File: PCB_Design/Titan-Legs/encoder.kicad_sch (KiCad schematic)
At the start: 2 parts, among them U2 AS5047P-ATSM

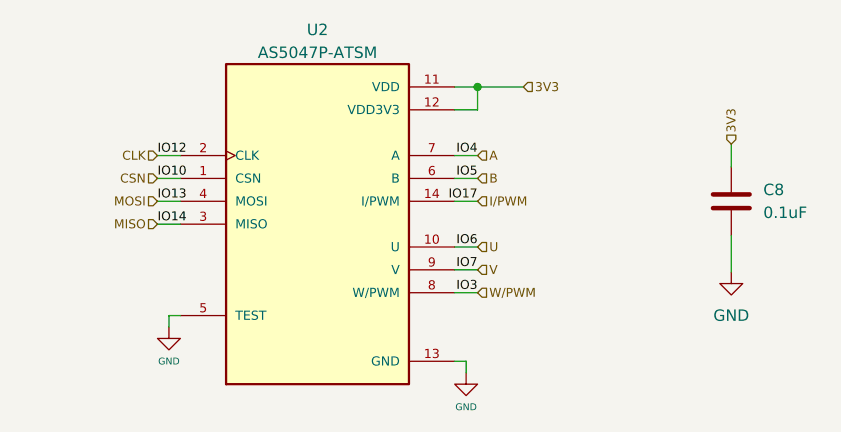
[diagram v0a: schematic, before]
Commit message: Copper filled VM to mosfets
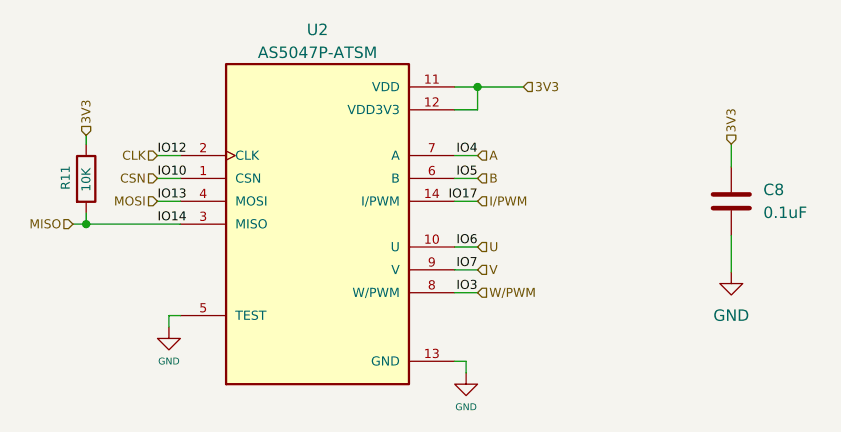
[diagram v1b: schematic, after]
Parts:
- added R11: 10K, Resistor_SMD:R_0603_1608Metric, symbol Device:R
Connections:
- net 3V3: now also R11.1
- net MISO: now also R11.2
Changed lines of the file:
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@@
   (junction (at 139.7 77.47) (diameter 0) (color 0 0 0 0)
   )
+  (junction (at 96.2152 92.71) (diameter 0) (color 0 0 0 0)
+  )
   (wire (pts (xy 105.41 102.87) (xy 105.41 104.14))
     (stroke (width 0) (type default) (color 0 0 0 0))
@@
     (stroke (width 0) (type default) (color 0 0 0 0))
   )
+  (wire (pts (xy 96.2152 82.8548) (xy 96.2152 83.8708))
+    (stroke (width 0) (type default) (color 0 0 0 0))
+  )
   (wire (pts (xy 139.7 77.47) (xy 144.78 77.47))
     (stroke (width 0) (type default) (color 0 0 0 0))
@@
     (stroke (width 0) (type default) (color 0 0 0 0))
   )
-  (wire (pts (xy 104.14 92.71) (xy 106.68 92.71))
+  (wire (pts (xy 96.2152 91.4908) (xy 96.2152 92.71))
+    (stroke (width 0) (type default) (color 0 0 0 0))
+  )
+  (wire (pts (xy 94.742 92.71) (xy 96.2152 92.71))
     (stroke (width 0) (type default) (color 0 0 0 0))
   )
@@
     (stroke (width 0) (type default) (color 0 0 0 0))
   )
+  (wire (pts (xy 96.2152 92.71) (xy 106.68 92.71))
+    (stroke (width 0) (type default) (color 0 0 0 0))
+  )
   (wire (pts (xy 138.43 107.95) (xy 138.43 109.22))
     (stroke (width 0) (type default) (color 0 0 0 0))
@@
     (effects (font (size 1 1)) (justify left))
   )
+  (hierarchical_label "3V3" (shape input) (at 96.2152 82.8548 90)
+    (effects (font (size 1 1)) (justify left))
+  )
   (hierarchical_label "3V3" (shape input) (at 144.78 77.47 0)
     (effects (font (size 1 1)) (justify left))
@@
     (effects (font (size 1 1)) (justify left))
   )
-  (hierarchical_label "MISO" (shape input) (at 104.14 92.71 180)
+  (hierarchical_label "MISO" (shape input) (at 94.742 92.71 180)
     (effects (font (size 1 1)) (justify right))
   )
@@
     (pin "1")
   )
+  (symbol (lib_id "Device:R") (at 96.2152 87.6808 0) (unit 1)
+    (in_bom yes) (on_board yes)
+    (property "Reference" "R11" (id 0) (at 93.9292 88.9 90)
+      (effects (font (size 1 1)) (justify left))
+    )
+    (property "Value" "10K" (id 1) (at 96.2152 89.1032 90)
+      (effects (font (size 1 1)) (justify left))
+    )
+    (property "Footprint" "Resistor_SMD:R_0603_1608Metric" (id 2) (at 94.4372 87.6808 90)
+      (effects (font (size 1.27 1.27)) hide)
+    )
+    (property "Datasheet" "~" (id 3) (at 96.2152 87.6808 0)
+      (effects (font (size 1.27 1.27)) hide)
+    )
+    (pin "1")
+    (pin "2")
+  )
 )

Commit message: Added Electrolytic Capacitor and moved AMS1117 to B.Cu
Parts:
- removed C8: 0.1uF, Capacitor_SMD:C_0603_1608Metric, symbol Device:C
- removed R11: 10K, Resistor_SMD:R_0603_1608Metric, symbol Device:R
- removed U2: AS5047P-ATSM, ENCODER:SOP65P640X120-14N, symbol AS5047P-ATSM:AS5047P-ATSM
